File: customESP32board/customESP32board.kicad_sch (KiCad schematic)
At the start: 50 parts, among them J1 USB_B, J2 Conn_01x16_Pin, J3 Conn_01x16_Pin, Q1 S8050, Q2 S8050, Q3 BSS138, Q4 BSS138, Q5 BSS138, SW1 SW_Push, SW2 SW_Push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

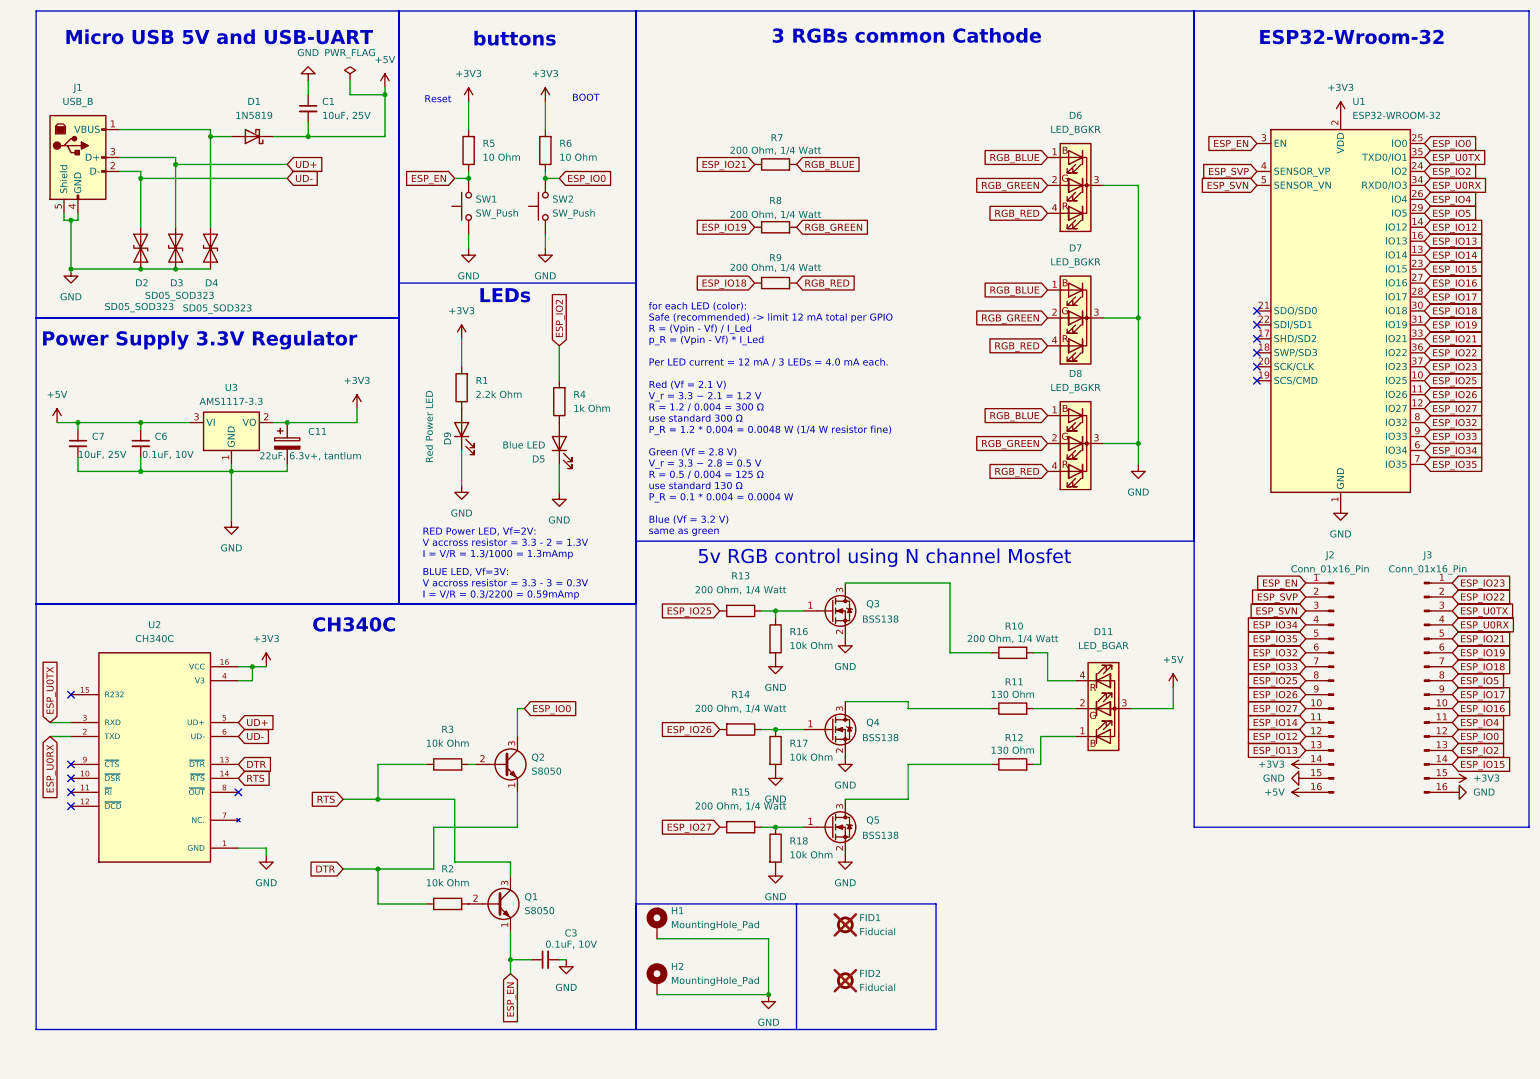
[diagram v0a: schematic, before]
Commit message: updated schematic
- changed pullup resistors from 10 to 10k
- updated ch340C bug and updated the capacitor on ESP reset pin (EN pin) to 10uF instead of 0.1uF
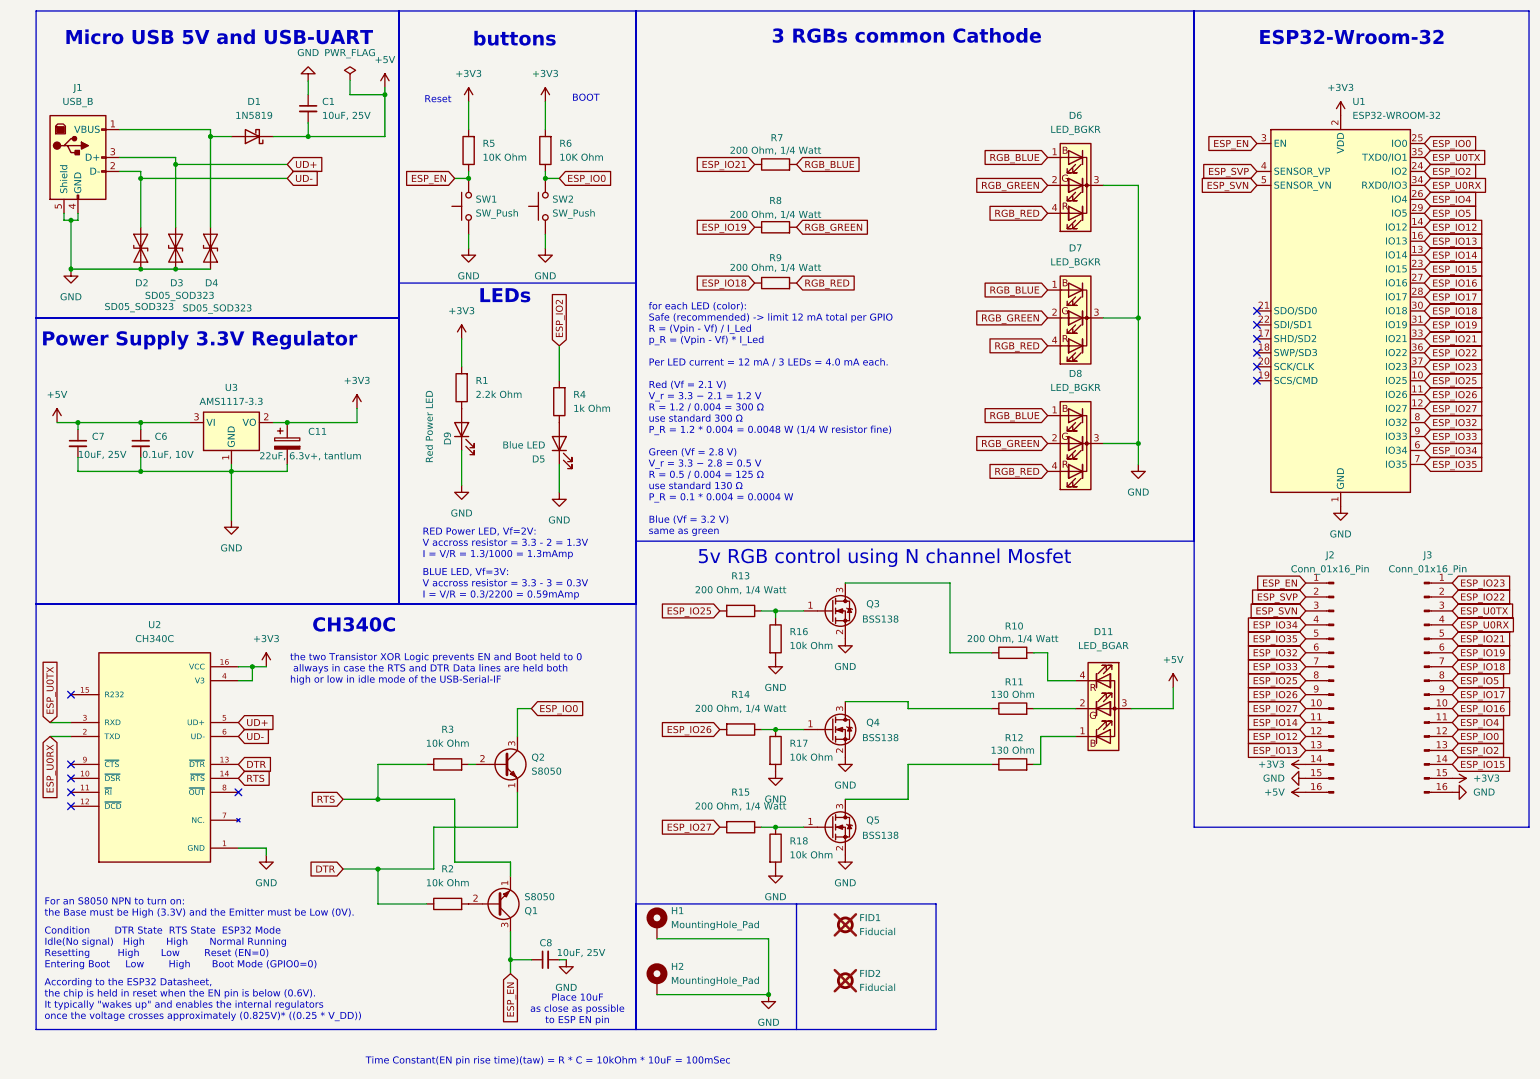
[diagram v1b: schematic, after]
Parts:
- removed C3: 0.1uF, 10V, Capacitor_SMD:C_0603_1608Metric, symbol Device:C_Small
- added C8: 10uF, 25V, Capacitor_SMD:C_0805_2012Metric, symbol Device:C_Small
- R5, R6: value 10 Ohm -> 10K Ohm
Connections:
- net ESP_EN: now also Q1.3 (C), C8.1; no longer Q1.1 (E)
- net GND: now also C8.2
- net RTS: now also Q1.1 (E); no longer Q1.3 (C)
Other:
- note added: "According to the ESP32 Datasheet, the chip is held in reset when the EN pin is below (0.6V). It typically "wakes up" and enables the internal regulators once the voltage crosses approximately (0.825V)* ((0.25 * V_DD))"
- note added: "Condition DTR State RTS State ESP32 Mode Idle(No signal) High High Normal Running Resetting High Low Reset (EN=0) Entering Boot Low High Boot Mode (GPIO0=0)"
- note added: "For an S8050 NPN to turn on: the Base must be High (3.3V) and the Emitter must be Low (0V)."
- note added: "Place 10uF as close as possible to ESP EN pin"
- note added: "Time Constant(EN pin rise time)(taw) = R * C = 10kOhm * 10uF = 100mSec"
- note added: "the two Transistor XOR Logic prevents EN and Boot held to 0 allways in case the RTS and DTR Data lines are held both high or low in idle mode of the USB-Serial-IF"

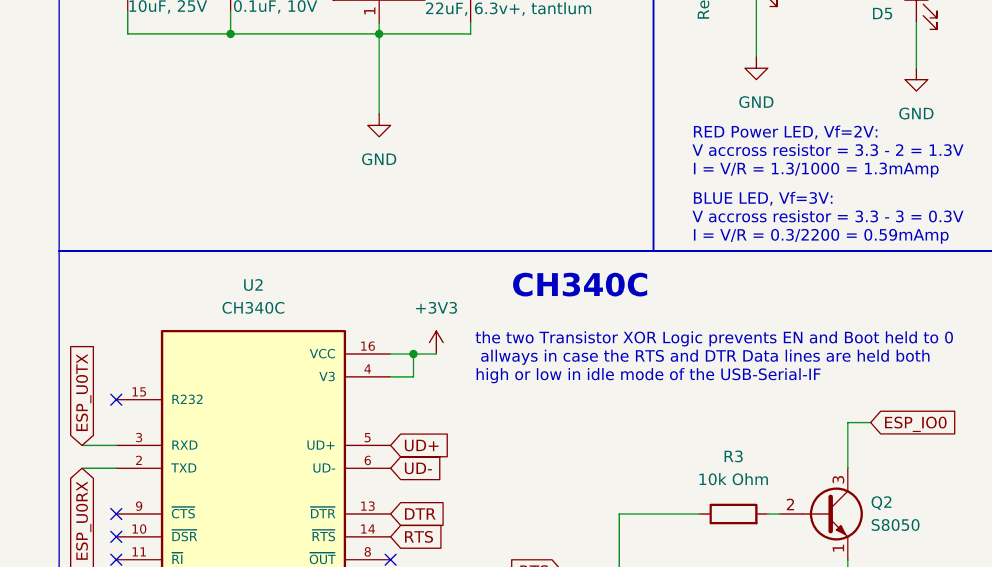
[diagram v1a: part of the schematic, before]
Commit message: added ESPtool reference
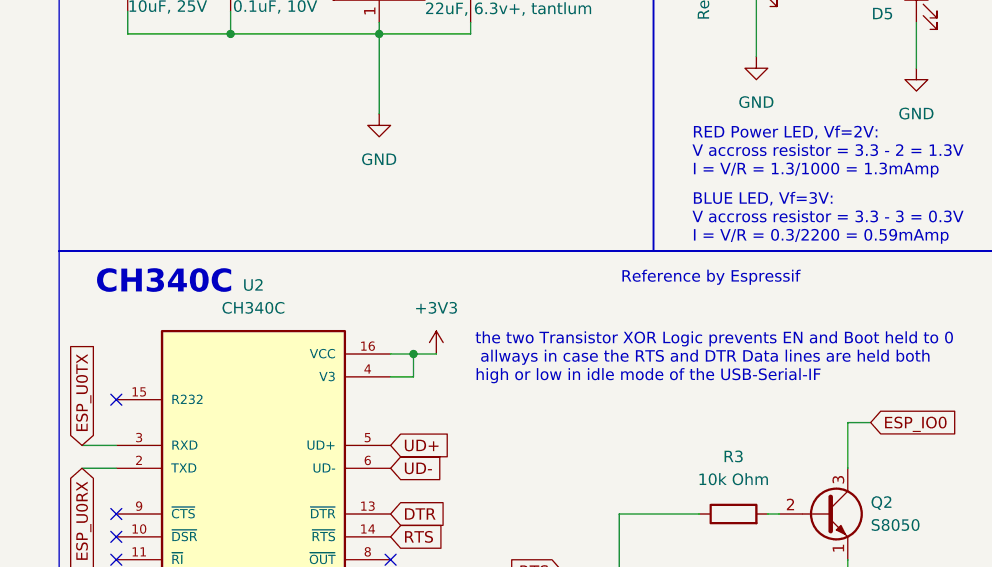
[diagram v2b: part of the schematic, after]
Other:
- note added: "Reference by Espressif"
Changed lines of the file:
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@@
+		)
+	)
+	(text "Reference by Espressif\n"
+		(exclude_from_sim no)
+		(at 85.09 123.698 0)
+		(effects
+			(font
+				(size 1.27 1.27)
+				(color 255 0 6 1)
+			)
+			(href "https://dl.espressif.com/dl/schematics/ESP32-Core-Board-V2_sch.pdf")
 		)
 	)
@@
 	(text "CH340C\n"
 		(exclude_from_sim no)
-		(at 70.612 124.714 0)
+		(at 24.384 124.206 0)
 		(effects
 			(font

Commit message: updated schematic
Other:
- note added: "In our case the S8050 NPN to turn on: the Base must be High (3.3V) and the Emitter must be Low (0V). V(BE) = 3.3V"
- note added: "Reference circuit by Espressif"
- note added: "actual IC calc IC = (Vcc - V(CEsat))/10k IC = (3.3 - 0.5) / 10k IC = 28mA"
- note added: "maximum current handling capability (ICmax) IB = (3.3v - V(BEon)) /10k = 0.23mA IC = IB * gain(hfe)worst case IC = 0.23mA * 45(worst case) IC = 1.03 A MAX current"
- note added: "the two Transistor XOR Logic prevents EN and Boot held to 0 always in case the RTS and DTR Data lines are held both high or low in idle mode of the USB-Serial-IF"
- note removed: "For an S8050 NPN to turn on: the Base must be High (3.3V) and the Emitter must be Low (0V)."
- note removed: "Reference by Espressif"
- note removed: "the two Transistor XOR Logic prevents EN and Boot held to 0 allways in case the RTS and DTR Data lines are held both high or low in idle mode of the USB-Serial-IF"
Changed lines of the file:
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@@
 		)
 	)
-	(text "Reference by Espressif\n"
+	(text "Reference circuit by Espressif\n"
 		(exclude_from_sim no)
-		(at 85.09 123.698 0)
+		(at 81.026 122.428 0)
 		(effects
 			(font
@@
 		)
 	)
-	(text "the two Transistor XOR Logic prevents EN and Boot held to 0\n allways in case the RTS and DTR Data lines are held both \nhigh or low in idle mode of the USB-Serial-IF"
+	(text "the two Transistor XOR Logic prevents EN and Boot held to 0\nalways in case the RTS and DTR Data lines are held both \nhigh or low in idle mode of the USB-Serial-IF"
 		(exclude_from_sim no)
-		(at 58.928 132.588 0)
+		(at 58.674 127 0)
 		(effects
 			(font
@@
 		)
 	)
-	(text "For an S8050 NPN to turn on:\nthe Base must be High (3.3V) and the Emitter must be Low (0V)."
+	(text "In our case the S8050 NPN to turn on:\nthe Base must be High (3.3V) and \nthe Emitter must be Low (0V).\nV(BE) = 3.3V"
 		(exclude_from_sim no)
-		(at 14.224 176.022 0)
+		(at 14.732 174.244 0)
 		(effects
 			(font
@@
 		)
 	)
+	(text "actual IC calc\nIC = (Vcc - V(CEsat))/10k\nIC = (3.3 - 0.5) / 10k\nIC = 28mA"
+		(exclude_from_sim no)
+		(at 58.674 145.288 0)
+		(effects
+			(font
+				(size 1.27 1.27)
+			)
+			(justify left)
+		)
+	)
 	(text "RED Power LED, Vf=2V:\nV accross resistor = 3.3 - 2 = 1.3V\nI = V/R = 1.3/1000 = 1.3mAmp"
 		(exclude_from_sim no)
@@
 		)
 	)
+	(text "maximum current handling capability (ICmax)\nIB = (3.3v - V(BEon)) /10k = 0.23mA\nIC = IB * gain(hfe)worst case\nIC = 0.23mA * 45(worst case)\nIC = 1.03 A MAX current"
+		(exclude_from_sim no)
+		(at 58.674 136.144 0)
+		(effects
+			(font
+				(size 1.27 1.27)
+			)
+			(justify left)
+		)
+	)
 	(junction
 		(at 147.32 143.51)
@@
 	(wire
 		(pts
-			(xy 49.53 165.1) (xy 54.61 165.1)
+			(xy 49.53 165.1) (xy 55.88 165.1)
 		)
 		(stroke
@@
 	(wire
 		(pts
-			(xy 54.61 165.1) (xy 54.61 166.37)
+			(xy 55.88 165.1) (xy 55.88 166.37)
 		)
 		(stroke
@@
 	(symbol
 		(lib_id "power:GND")
-		(at 54.61 166.37 0)
+		(at 55.88 166.37 0)
 		(unit 1)
 		(body_style 1)
@@
 		(fields_autoplaced yes)
 		(property "Reference" "#PWR05"
-			(at 54.61 172.72 0)
+			(at 55.88 172.72 0)
 			(hide yes)
 			(show_name no)
@@
 		)
 		(property "Value" "GND"
-			(at 54.61 171.45 0)
+			(at 55.88 171.45 0)
 			(show_name no)
 			(do_not_autoplace no)
@@
 		)
 		(property "Footprint" ""
-			(at 54.61 166.37 0)
+			(at 55.88 166.37 0)
 			(hide yes)
 			(show_name no)
@@
 		)
 		(property "Datasheet" ""
-			(at 54.61 166.37 0)
+			(at 55.88 166.37 0)
 			(hide yes)
 			(show_name no)
@@
 		)
 		(property "Description" "Power symbol creates a global label with name \"GND\" , ground"
-			(at 54.61 166.37 0)
+			(at 55.88 166.37 0)
 			(hide yes)
 			(show_name no)

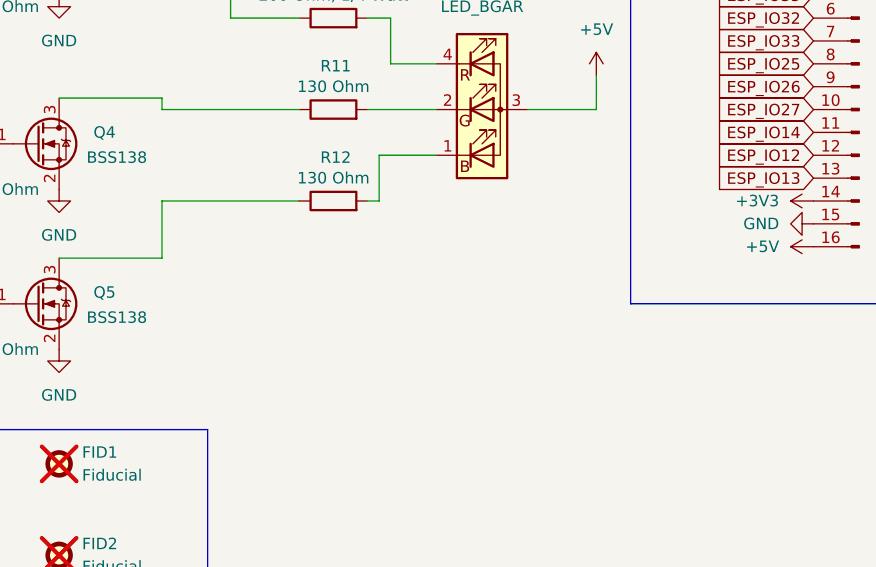
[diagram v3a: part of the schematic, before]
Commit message: documented esp32 calc of led nmos
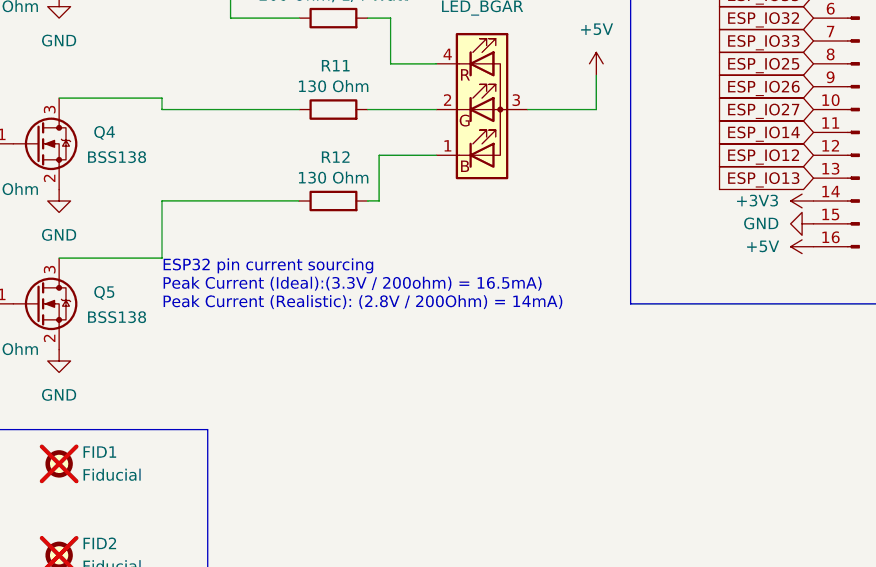
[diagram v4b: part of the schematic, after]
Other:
- note added: "ESP32 pin current sourcing Peak Current (Ideal):(3.3V / 200ohm) = 16.5mA) Peak Current (Realistic): (2.8V / 200Ohm) = 14mA)"
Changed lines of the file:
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@@
+		)
+	)
+	(text "ESP32 pin current sourcing\nPeak Current (Ideal):(3.3V / 200ohm) = 16.5mA)\nPeak Current (Realistic): (2.8V / 200Ohm) = 14mA)"
+		(exclude_from_sim no)
+		(at 171.45 159.258 0)
+		(effects
+			(font
+				(size 1.27 1.27)
+			)
+			(justify left)
 		)
 	)
